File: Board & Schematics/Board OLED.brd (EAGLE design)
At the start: 25.4 x 25.4 mm, 23 parts

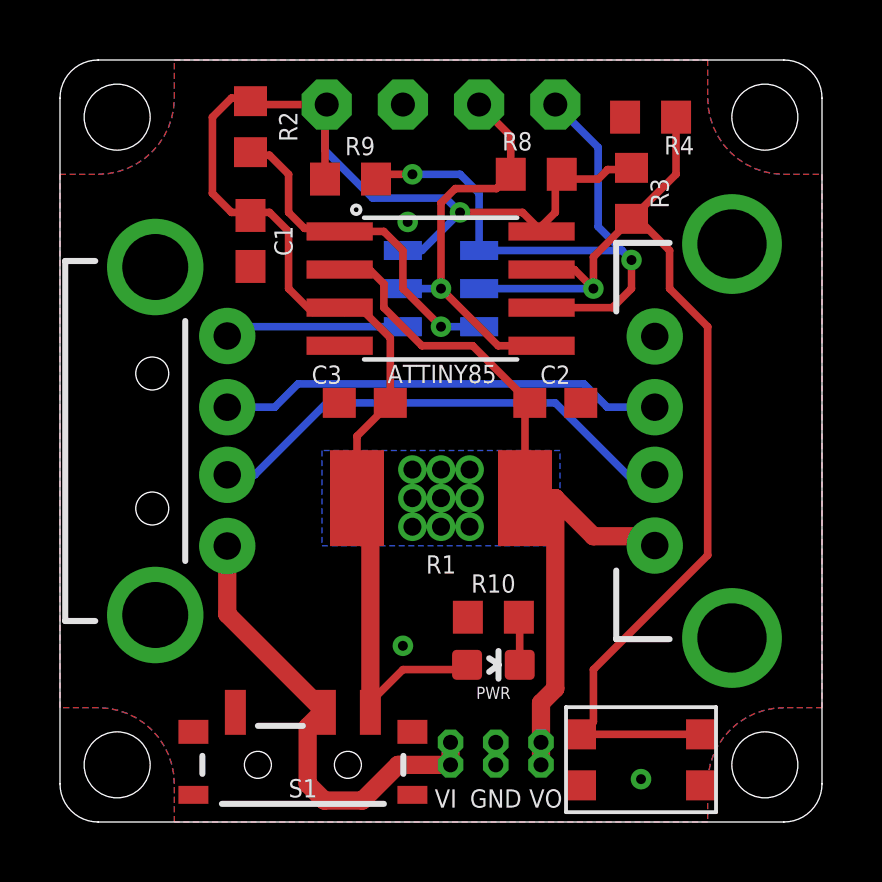
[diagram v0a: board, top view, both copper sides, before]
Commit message: Switch GND/VCC pinout for different OLED display
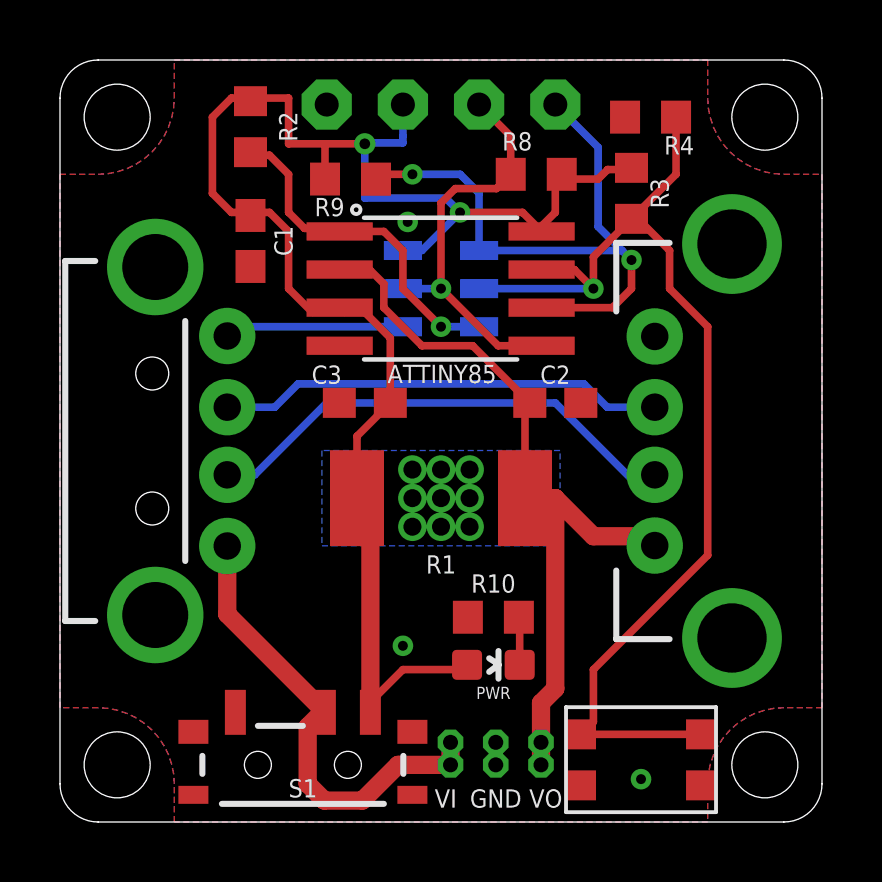
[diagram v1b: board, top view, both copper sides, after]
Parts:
- U$2: value OLED-I2C -> OLED-I2CGND-VCC-SCL-SDA
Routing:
- net +5V: track 52.8 -> 55.7 mm, vias 1 -> 2
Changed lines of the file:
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@@
 <?xml version="1.0" encoding="utf-8"?>
 <!DOCTYPE eagle SYSTEM "eagle.dtd">
-<eagle version="6.5.0">
+<eagle version="7.5.0">
 <drawing>
 <settings>
@@
 <setting verticaltext="up"/>
 </settings>
-<grid distance="0.05" unitdist="inch" unit="mil" style="lines" multiple="1" display="yes" altdistance="6.25" altunitdist="mil" altunit="mil"/>
+<grid distance="0.01" unitdist="inch" unit="inch" style="lines" multiple="1" display="yes" altdistance="0.0025" altunitdist="inch" altunit="inch"/>
 <layers>
 <layer number="1" name="Top" color="4" fill="1" visible="yes" active="yes"/>
@@
 <layer number="27" name="tValues" color="7" fill="1" visible="no" active="yes"/>
 <layer number="28" name="bValues" color="7" fill="1" visible="no" active="yes"/>
-<layer number="29" name="tStop" color="7" fill="3" visible="yes" active="yes"/>
-<layer number="30" name="bStop" color="7" fill="6" visible="yes" active="yes"/>
-<layer number="31" name="tCream" color="7" fill="4" visible="yes" active="yes"/>
-<layer number="32" name="bCream" color="7" fill="5" visible="yes" active="yes"/>
-<layer number="33" name="tFinish" color="6" fill="3" visible="yes" active="yes"/>
-<layer number="34" name="bFinish" color="6" fill="6" visible="yes" active="yes"/>
-<layer number="35" name="tGlue" color="7" fill="4" visible="yes" active="yes"/>
-<layer number="36" name="bGlue" color="7" fill="5" visible="yes" active="yes"/>
-<layer number="37" name="tTest" color="7" fill="1" visible="yes" active="yes"/>
-<layer number="38" name="bTest" color="7" fill="1" visible="yes" active="yes"/>
+<layer number="29" name="tStop" color="7" fill="3" visible="no" active="yes"/>
+<layer number="30" name="bStop" color="7" fill="6" visible="no" active="yes"/>
+<layer number="31" name="tCream" color="7" fill="4" visible="no" active="yes"/>
+<layer number="32" name="bCream" color="7" fill="5" visible="no" active="yes"/>
+<layer number="33" name="tFinish" color="6" fill="3" visible="no" active="yes"/>
+<layer number="34" name="bFinish" color="6" fill="6" visible="no" active="yes"/>
+<layer number="35" name="tGlue" color="7" fill="4" visible="no" active="yes"/>
+<layer number="36" name="bGlue" color="7" fill="5" visible="no" active="yes"/>
+<layer number="37" name="tTest" color="7" fill="1" visible="no" active="yes"/>
+<layer number="38" name="bTest" color="7" fill="1" visible="no" active="yes"/>
 <layer number="39" name="tKeepout" color="4" fill="11" visible="yes" active="yes"/>
 <layer number="40" name="bKeepout" color="1" fill="11" visible="yes" active="yes"/>
@@
 <layer number="59" name="tCarbon" color="7" fill="1" visible="no" active="no"/>
 <layer number="60" name="bCarbon" color="7" fill="1" visible="no" active="no"/>
-<layer number="90" name="Modules" color="5" fill="1" visible="yes" active="yes"/>
+<layer number="90" name="Modules" color="5" fill="1" visible="no" active="no"/>
 <layer number="91" name="Nets" color="2" fill="1" visible="no" active="no"/>
 <layer number="92" name="Busses" color="1" fill="1" visible="no" active="no"/>
@@
 <pass name="Default">
 <param name="RoutingGrid" value="50mil"/>
+<param name="AutoGrid" value="1"/>
+<param name="Efforts" value="0"/>
+<param name="TopRouterVariant" value="1"/>
 <param name="tpViaShape" value="round"/>
 <param name="PrefDir.1" value="|"/>
@@
 <attribute name="VALUE" x="10.795" y="15.875" size="1.27" layer="27" rot="R180"/>
 </element>
-<element name="U$2" library="OwnStuff" package="OLED-I2C" value="OLED-I2C" x="12.7" y="12.065"/>
+<element name="U$2" library="OwnStuff" package="OLED-I2C" value="OLED-I2CGND-VCC-SCL-SDA" x="12.7" y="12.065"/>
 <element name="R8" library="rcl" package="R0603" value="10kΩ" x="15.875" y="21.59" smashed="yes">
 <attribute name="NAME" x="15.24" y="22.38375" size="0.6096" layer="25" align="bottom-center"/>
@@
 </element>
 <element name="R9" library="rcl" package="R0603" value="10kΩ" x="9.68375" y="21.43125" smashed="yes" rot="R180">
-<attribute name="NAME" x="10.00125" y="22.225" size="0.6096" layer="25" rot="R180" align="top-center"/>
+<attribute name="NAME" x="8.98525" y="20.193" size="0.6096" layer="25" rot="R180" align="top-center"/>
 <attribute name="VALUE" x="10.31875" y="23.33625" size="1.27" layer="27" rot="R180"/>
 </element>
@@
 <contactref element="PWR" pad="A"/>
 <contactref element="C3" pad="1"/>
-<wire x1="8.89" y1="23.915" x2="6.4625" y2="23.915" width="0.254" layer="1"/>
 <wire x1="6.4625" y1="23.915" x2="6.35" y2="24.0275" width="0.254" layer="1"/>
 <wire x1="5.08" y1="23.495" x2="5.715" y2="24.13" width="0.254" layer="1"/>
@@
 <wire x1="16.51" y1="20.32" x2="16.51" y2="21.375" width="0.254" layer="1"/>
 <wire x1="16.51" y1="21.375" x2="16.725" y2="21.59" width="0.254" layer="1"/>
-<wire x1="8.83375" y1="21.43125" x2="8.83375" y2="23.85875" width="0.254" layer="1"/>
-<wire x1="8.83375" y1="23.85875" x2="8.89" y2="23.915" width="0.254" layer="1"/>
 <wire x1="6.35" y1="20.2175" x2="6.35" y2="20.32" width="0.254" layer="1"/>
-<wire x1="10.42125" y1="20.79625" x2="8.83375" y2="22.38375" width="0.254" layer="16"/>
-<wire x1="8.83375" y1="22.38375" x2="8.83375" y2="23.85875" width="0.254" layer="16"/>
-<wire x1="8.83375" y1="23.85875" x2="8.89" y2="23.915" width="0.254" layer="16"/>
-<wire x1="10.42125" y1="20.79625" x2="12.85875" y2="20.79625" width="0.254" layer="16"/>
+<wire x1="11.43" y1="22.86" x2="11.43" y2="23.915" width="0.254" layer="16"/>
+<wire x1="10.16" y1="20.79625" x2="12.85875" y2="20.79625" width="0.254" layer="16"/>
 <wire x1="12.85875" y1="20.79625" x2="13.335" y2="20.32" width="0.254" layer="16"/>
 <wire x1="11.43" y1="19.05" x2="12.065" y2="19.05" width="0.254" layer="16"/>
 <wire x1="12.065" y1="19.05" x2="13.335" y2="20.32" width="0.254" layer="16"/>
+<wire x1="8.83375" y1="21.43125" x2="8.89" y2="21.43125" width="0.254" layer="1"/>
+<wire x1="8.89" y1="21.336" x2="8.89" y2="21.43125" width="0.254" layer="1"/>
+<wire x1="11.43" y1="22.63775" x2="11.43" y2="22.86" width="0.254" layer="16"/>
+<wire x1="11.43" y1="22.63775" x2="10.16" y2="22.63775" width="0.254" layer="16"/>
+<wire x1="10.16" y1="22.63775" x2="10.16" y2="22.606" width="0.254" layer="16"/>
+<via x="10.16" y="22.606" extent="1-16" drill="0.3556" shape="octagon"/>
+<wire x1="10.16" y1="22.606" x2="8.89" y2="22.606" width="0.254" layer="1"/>
+<wire x1="8.89" y1="22.606" x2="8.83375" y2="22.606" width="0.254" layer="1"/>
+<wire x1="8.83375" y1="22.606" x2="8.83375" y2="21.43125" width="0.254" layer="1"/>
+<wire x1="10.16" y1="20.79625" x2="10.16" y2="22.606" width="0.254" layer="16"/>
+<wire x1="6.4625" y1="23.915" x2="6.35" y2="23.915" width="0.254" layer="1"/>
+<wire x1="6.35" y1="23.915" x2="6.35" y2="24.13" width="0.254" layer="1"/>
+<wire x1="6.35" y1="24.13" x2="7.62" y2="24.13" width="0.254" layer="1"/>
+<wire x1="7.62" y1="24.13" x2="7.62" y2="22.606" width="0.254" layer="1"/>
+<wire x1="7.62" y1="22.606" x2="8.83375" y2="22.606" width="0.254" layer="1"/>
 </signal>
 <signal name="RST">
